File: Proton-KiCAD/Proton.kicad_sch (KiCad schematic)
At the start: 44 parts, among them J1 USB_C_Receptacle_USB2.0_14P, J9 Conn_01x03_Pin, SW1 BOOTSEL, SW2 RESET, U1 W25Q128JVS, U2 USBLC6-2P6, U3 NCP1117-3.3_SOT223, U4 RP2350_80QFN, Y1 ABM8-272-T3

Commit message: ready for final check
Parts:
- added C34, C35: 22uF, Capacitor_SMD:C_0805_2012Metric, symbol Device:C
- added J10: BATTERY IN, Connector_PinHeader_2.54mm:PinHeader_1x02_P2.54mm_Vertical, symbol Connector:Conn_01x02_Pin
- added U7: AMS1117-5.0, Package_TO_SOT_SMD:SOT-223-3_TabPin2, symbol Regulator_Linear:AMS1117-5.0
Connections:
- net GND: now also C34.2, C35.2, J10.2 (Pin_2), U7.1 (GND)
- net VBUS: now also C35.1, U7.2 (VO)
- net GPIO12 renamed FRONT_BUTTON_1
- net GPIO13 renamed FRONT_BUTTON_2
- new net: C34.1, J10.1 (Pin_1), U7.3 (VI)
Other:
- note added: "Battery Input"
- note removed: "Debugger Sheet (Link)"

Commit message: Finished
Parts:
- added J14: DEBUGGER, Connector_PinHeader_2.54mm:PinHeader_1x03_P2.54mm_Vertical, symbol Connector:Conn_01x03_Pin
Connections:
- net GND: now also J14.3 (Pin_3)
- net SWCLK: now also J14.1 (Pin_1)
- net SWD: now also J14.2 (Pin_2)
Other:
- note added: "Rechargable Battery Input"
- note removed: "(Due to RP2350-E9 errata on the A2 stepping, a weaker pull-down is necessary to ensure the pin will go back down to zero when the button is pressed.)"
- note removed: "User Buttons"
- note removed: "User LEDs"
- moved on the sheet: C34, C35, J10, U7

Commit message: changed audio section
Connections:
- net GPIO42_ADC2 renamed RF_AUDIO_2
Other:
- added sheet Audio Section (Proton_Audio.kicad_sch)
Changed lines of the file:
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@@
 	(wire
 		(pts
-			(xy 232.41 234.95) (xy 247.65 234.95)
+			(xy 232.41 234.95) (xy 254 234.95)
 		)
 		(stroke
@@
 		)
 	)
+	(global_label "RF_AUDIO_2"
+		(shape input)
+		(at 254 234.95 0)
+		(fields_autoplaced yes)
+		(effects
+			(font
+				(size 1.27 1.27)
+			)
+			(justify left)
+		)
+		(property "Intersheetrefs" "${INTERSHEET_REFS}"
+			(at 267.4587 234.95 0)
+			(effects
+				(font
+					(size 1.27 1.27)
+				)
+				(justify left)
+				(hide yes)
+			)
+		)
+	)
 	(global_label "OLED_SPI0_TX"
 		(shape input)
@@
 	)
 	(sheet
-		(at 347.98 144.78)
+		(at 360.68 166.37)
+		(size 21.59 21.59)
+		(exclude_from_sim no)
+		(in_bom yes)
+		(on_board yes)
+		(dnp no)
+		(fields_autoplaced yes)
+		(stroke
+			(width 0.1524)
+			(type solid)
+		)
+		(fill
+			(color 0 0 0 0.0000)
+		)
+		(property "Sheetname" "Audio Section"
+			(at 360.68 165.6584 0)
+			(effects
+				(font
+					(size 1.27 1.27)
+				)
+				(justify left bottom)
+			)
+		)
+		(property "Sheetfile" "Proton_Audio.kicad_sch"
+			(at 360.68 188.5446 0)
+			(effects
+				(font
+					(size 1.27 1.27)
+				)
+				(justify left top)
+			)
+		)
+		(instances
+			(project "Proton"
+				(path "/94683f5c-9cd9-448e-be96-9792537b5cb8"
+					(page "3")
+				)
+			)
+		)
+	)
+	(sheet
+		(at 346.71 123.19)
 		(size 25.4 19.05)
 		(exclude_from_sim no)
@@
 		)
 		(property "Sheetname" "SSTV PERIPHERALS"
-			(at 347.98 144.0684 0)
+			(at 346.71 122.4784 0)
 			(effects
 				(font
@@
 		)
 		(property "Sheetfile" "untitled.kicad_sch"
-			(at 347.98 164.4146 0)
+			(at 346.71 142.8246 0)
 			(effects
 				(font

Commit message: finished updated layout
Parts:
- renumbered C8 to C10, C9 to C11, C10 to C12, C11 to C13, C12 to C14, C13 to C15, C14 to C16, C15 to C17, C16 to C18, C17 to C19, C18 to C20, C19 to C21, C20 to C22, C21 to C23, C34 to C3, C3 to C4, C35 to C5, C4 to C6, C5 to C7, C6 to C8, C7 to C9, J10 to J1, J1 to J2, J14 to J3, J9 to J4, U7 to U1, U1 to U2, U2 to U3, U3 to U4, U4 to U5

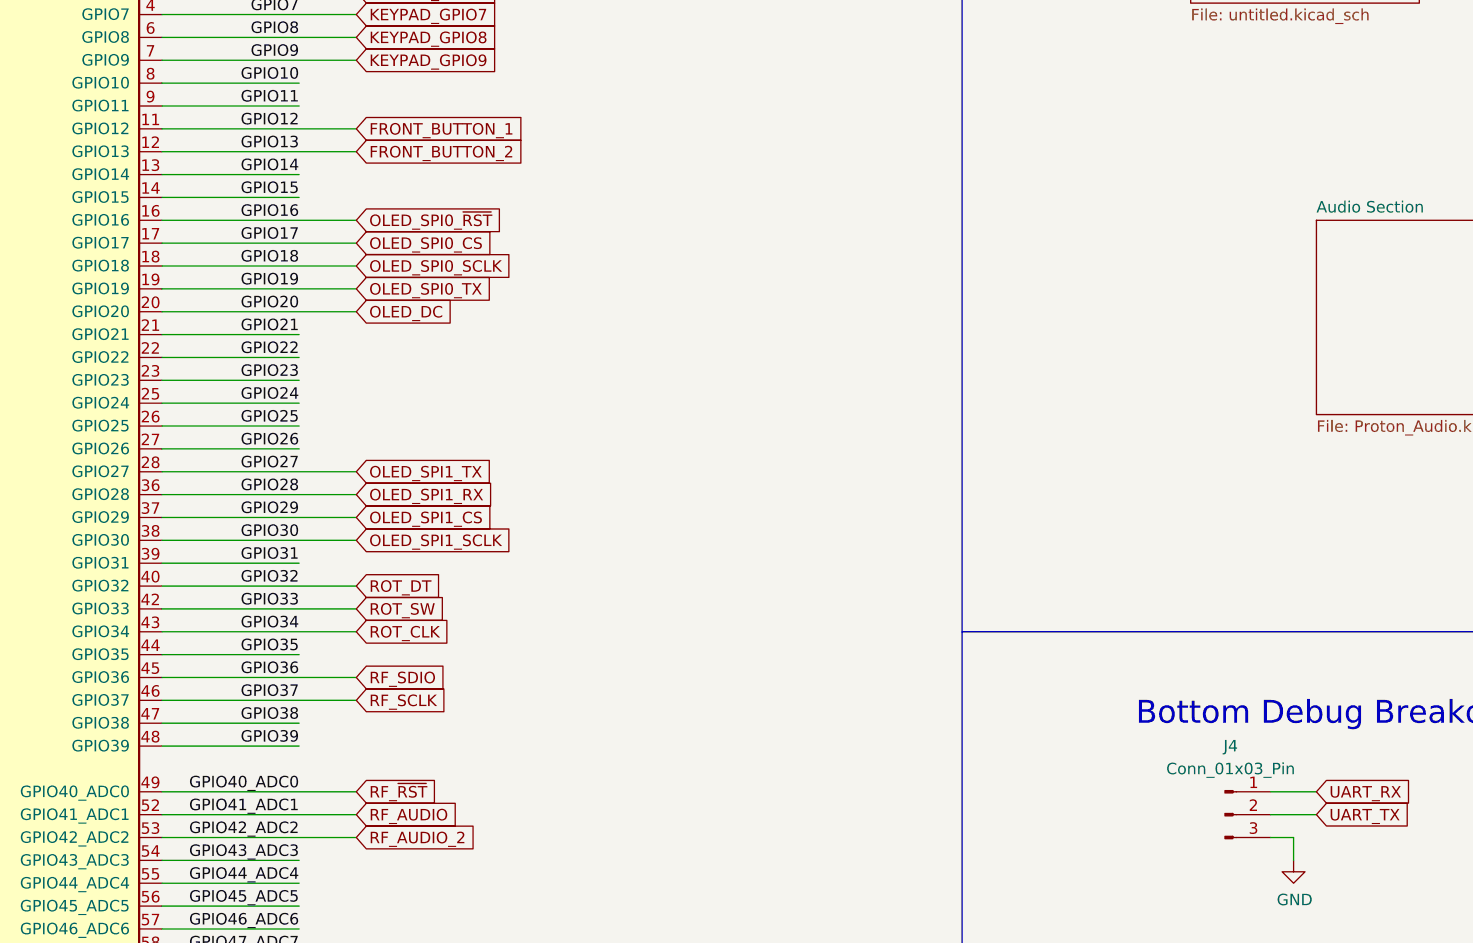
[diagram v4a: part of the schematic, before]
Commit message: BOM and CPL changes
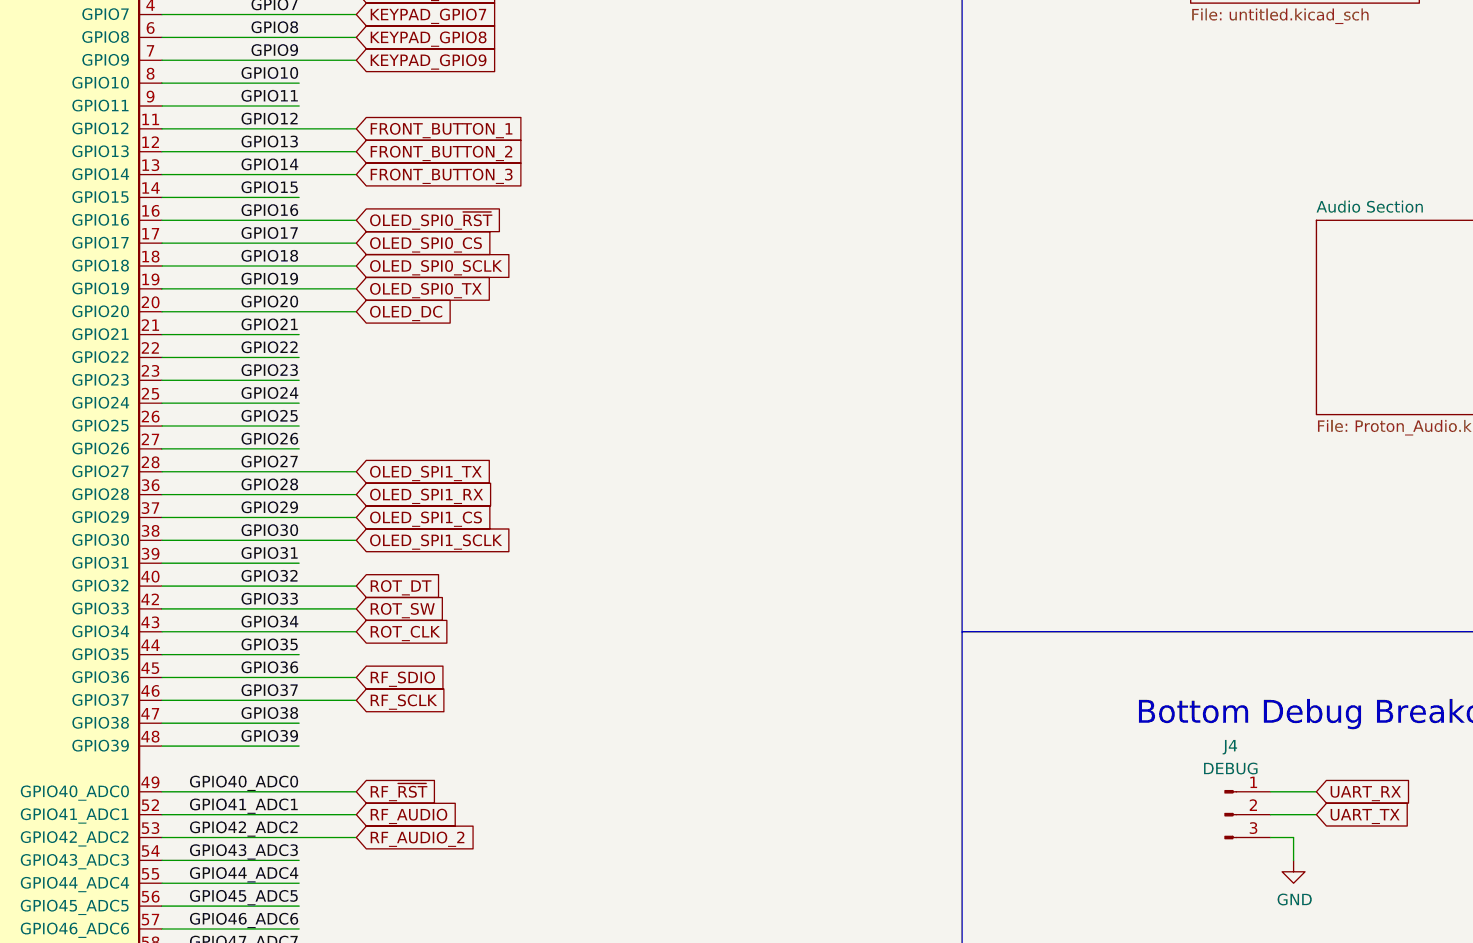
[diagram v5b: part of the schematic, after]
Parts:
- J4: value Conn_01x03_Pin -> DEBUG
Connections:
- net GPIO14 renamed FRONT_BUTTON_3
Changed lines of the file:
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@@
 	(wire
 		(pts
-			(xy 232.41 161.29) (xy 247.65 161.29)
+			(xy 232.41 161.29) (xy 254 161.29)
 		)
 		(stroke
@@
 		)
 	)
+	(global_label "FRONT_BUTTON_3"
+		(shape input)
+		(at 254 161.29 0)
+		(fields_autoplaced yes)
+		(effects
+			(font
+				(size 1.27 1.27)
+			)
+			(justify left)
+		)
+		(property "Intersheetrefs" "${INTERSHEET_REFS}"
+			(at 272.6596 161.29 0)
+			(effects
+				(font
+					(size 1.27 1.27)
+				)
+				(justify left)
+				(hide yes)
+			)
+		)
+	)
 	(global_label "RF_AUDIO"
 		(shape input)
@@
 			)
 		)
-		(property "Value" "Conn_01x03_Pin"
+		(property "Value" "DEBUG"
 			(at 351.155 227.33 0)
 			(effects
